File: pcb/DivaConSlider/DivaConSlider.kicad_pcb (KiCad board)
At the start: 2 copper layers, 548 x 97 mm, 225 parts, among them J1 HS96L03W2C03, J2 B8B-PH-SM4-TB, U1 MPR121QR2, U2 MPR121QR2, U3 MPR121QR2, U4 MPR121QR2, U5 74AHCT1G14

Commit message: revision 1.1 pcb schematics and layout
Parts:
- R17: value 330R -> 470R
- U5: value 74AHCT1G14 -> 74HCT1G14
- moved R5 8.00 mm to (96.0, 139.8)
- moved TP10 5.70 mm to (84.0, 145.0)
- moved R6 4.00 mm to (94.0, 139.8)
- moved TP11 3.75 mm to (79.8, 140.5)
- moved C13 3.32 mm to (88.0, 139.8), turned to -90 degrees
- moved C6 2.94 mm to (84.0, 139.8), turned to -90 degrees
- moved TP12 2.47 mm to (87.2, 148.2)
- moved R7 2.00 mm to (90.0, 139.8)
- moved R8 2.00 mm to (92.0, 139.8)
- moved C12 1.98 mm to (86.5, 139.8), turned to -90 degrees
- moved C7 1.49 mm to (82.5, 139.8), turned to -90 degrees
- renumbered C78 to C14, C14 to C15, C15 to C16, C16 to C17, C17 to C18, C18 to C19, C19 to C20, C20 to C21, C21 to C22, C22 to C23, C23 to C24, C24 to C25, C25 to C26, C26 to C27, C27 to C28, C28 to C29, C29 to C30, C30 to C31, C31 to C32, C32 to C33, C33 to C34, C34 to C35, C35 to C36, C36 to C37, C37 to C38, C38 to C39, C39 to C40, C40 to C41, C41 to C42, C42 to C43, C43 to C44, C44 to C45, C45 to C46, C46 to C47, C47 to C48, C48 to C49, C49 to C50, C50 to C51, C51 to C52, C52 to C53, C53 to C54, C54 to C55, C55 to C56, C56 to C57, C57 to C58, C58 to C59, C59 to C60, C60 to C61, C61 to C62, C62 to C63, C63 to C64, C64 to C65, C65 to C66, C66 to C67, C67 to C68, C68 to C69, C69 to C70, C70 to C71, C71 to C72, C72 to C73, C73 to C74, C74 to C75, C75 to C76, C76 to C77, C77 to C78, R2 to R1, R1 to R2, TP14 to TP1, TP1 to TP10, TP8 to TP11, TP9 to TP12, TP11 to TP13, TP5 to TP2, TP2 to TP3, TP3 to TP4, TP4 to TP5, TP7 to TP6, TP12 to TP7, TP6 to TP8, TP13 to TP9
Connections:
- J2 pad 1: GND -> Net-(J2-Pin_1)
- J2 pad 5: Net-(J2-Pin_5) -> +3V3
- J2 pad 6: /LED_DATA -> GND
- J2 pad 7: +3V3 -> +5V
- J2 pad 8: +5V -> /LED_DATA
- R5 pad 1: Net-(J2-Pin_5) -> Net-(J2-Pin_1)
- R5 pad 2: /I2C_SCL -> /DISPLAY_I2C_SCL
- R6 pad 1: Net-(J2-Pin_4) -> Net-(J2-Pin_2)
- R6 pad 2: /I2C_SDA -> /DISPLAY_I2C_SDA
- R7 pad 2: /DISPLAY_I2C_SDA -> /I2C_SCL
- R8 pad 1: Net-(J2-Pin_2) -> Net-(J2-Pin_4)
- R8 pad 2: /DISPLAY_I2C_SCL -> /I2C_SDA
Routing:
- net +5V: track 955.6 -> 977.3 mm
- net Net-(J2-Pin_5): track 6.50 -> 0.00 mm
- net Net-(J2-Pin_1): track 0.00 -> 6.50 mm
- net /LED_DATA: track 17.3 -> 12.6 mm, vias 2 -> 0
- net GND: track 828.8 -> 824.6 mm, vias 1320 -> 1439
- net /I2C_SCL: track 457.7 -> 460.0 mm
- net Net-(D1-DIN): track 57.9 -> 59.9 mm
- net /I2C_SDA: track 456.1 -> 457.8 mm
- net /DISPLAY_I2C_SDA: track 90.7 -> 89.7 mm
- net Net-(J2-Pin_4): track 6.50 -> 7.33 mm, vias 0 -> 2
- net Net-(J2-Pin_3): track 6.50 -> 7.33 mm

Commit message: Update PCBs to purchased revision
Main edit is using a ULN2003 NPN transistor array over discrete MOSFETs.
This was chosen because there was limited board space to put in
pull-down resistors on the board and it was complicating the single
layer routing. The PCB had to be expanded to 70x75mm anyways to
accommodate the SOIC ic anyways.

The schematics of the IO board were also updated to use net labels over
direct wiring. Due to the JST connectors and the Pi Pico schematic
symbol being mirrored, it was getting too difficult to have an
understandable schematic.

Minor edit was changing LED_DATA to nLED_DATA to signify that it is
an active low signal.
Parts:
- added R17: 10k, Resistor_SMD:R_0603_1608Metric, B.Cu at (74.8, 136.8)
- added SYM1: Logo_Open_Hardware_Small, Symbol:OSHW-Logo_5.7x6mm_SilkScreen, F.Cu at (394.0, 132.0)
- added SYM2: Leek, CustomLogos:Leek-Logo_6.3mm_Silkscreen, F.Cu at (388.0, 131.0)
- added TP14: TestPoint, TestPoint:TestPoint_Pad_D1.5mm, B.Cu at (155.8, 134.4)
- C12, C6: footprint Capacitor_SMD:C_0603_1608Metric -> Capacitor_SMD:C_0805_2012Metric
- H37, H38, H39, H40, H41, H42, H43, H44, H45: value Spacer_M3 -> Standoff_M3
- J2: value B8B-PH-SM4-TB -> B8B-PH-SM4-TBT
- U5: value 74HCT1G14 -> 74HCT1G14GV,125
- moved C7 1.00 mm to (81.5, 139.8)
- moved C12 0.53 mm to (86.0, 139.9)
- moved C6 0.53 mm to (83.5, 139.9)
- moved TP10 0.50 mm to (83.5, 145.0)
- moved TP11 0.25 mm to (79.5, 140.5)
- turned R10 to 45 degrees
- turned R11 to 45 degrees
- turned R9 to 45 degrees
- renumbered R17 to R18, R18 to R19, TP4 to TP2, TP5 to TP3, TP2 to TP4, TP3 to TP5
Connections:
- net /LED_DATA renamed /nLED_DATA
- H41 pad 1: (no net) -> unconnected-(H41-Pad1)
- H42 pad 1: (no net) -> unconnected-(H42-Pad1)
- H43 pad 1: (no net) -> unconnected-(H43-Pad1)
- H44 pad 1: (no net) -> unconnected-(H44-Pad1)
- H45 pad 1: (no net) -> unconnected-(H45-Pad1)
- R10 pad 1: Net-(U2-~{IRQ}) -> +3V3
- R10 pad 2: +3V3 -> Net-(U2-~{IRQ})
- R11 pad 1: Net-(U3-~{IRQ}) -> +3V3
- R11 pad 2: +3V3 -> Net-(U3-~{IRQ})
- R9 pad 1: Net-(U1-~{IRQ}) -> +3V3
- R9 pad 2: +3V3 -> Net-(U1-~{IRQ})
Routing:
- net +5V: track 977.3 -> 983.4 mm
- net GND: track 824.6 -> 829.4 mm, vias 1439 -> 1441
- net /nLED_DATA: track 12.6 -> 16.2 mm
- net +3V3: track 542.6 -> 544.7 mm
- net /I2C_SCL: track 460.0 -> 461.6 mm
- net /I2C_SDA: track 457.8 -> 459.2 mm
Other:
- board text added: "${TITLE} Rev. ${REVISION} ${ISSUE_DATE} ${COMPANY}"
- board text added: "DISPLAY SCL"
- board text added: "DISPLAY SDA"
- board text added: "LED DATA"
- board text added: "SLIDER SCL"
- board text added: "SLIDER SDA"
- board text added: "nDATA"
- board text removed: "${TITLE} Rev. ${REVISION} ${COMPANY} ${ISSUE_DATE}"

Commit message: Fix slider led_data silkscreen
Didn't indicate active low on the connector, had just "DATA" for the
test point, and had a redundant old silk screen label from a removed
test point location
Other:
- board text added: "LED_DATA"
- board text added: "nLED DATA"
- board text removed: "DATA"
- board text removed: "LED DATA"
- board text removed: "nDATA"
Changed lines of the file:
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@@
 	(title_block
 		(title "DivaCon Gold Slider")
-		(date "2025-11-14")
-		(rev "1.1")
+		(date "2025-11-21")
+		(rev "1.2")
 		(company "Alexander Knapik")
 	)
@@
 		)
 	)
-	(gr_text "LED DATA"
+	(gr_text "nLED DATA"
 		(at 82 127.75 270)
 		(layer "F.SilkS")
@@
 		)
 	)
-	(gr_text "DATA"
-		(at 28.25 163.75 0)
-		(layer "B.SilkS")
-		(effects
-			(font
-				(size 1.5 1.5)
-				(thickness 0.3)
-				(bold yes)
-			)
-			(justify mirror)
-		)
-	)
 	(gr_text "I2C: 0x5D"
 		(at 503 158.83 0)
@@
 		)
 	)
-	(gr_text "nDATA"
-		(at 71.736 148 90)
+	(gr_text "LED_DATA"
+		(at 71.736 150 90)
 		(layer "B.SilkS")
 		(effects

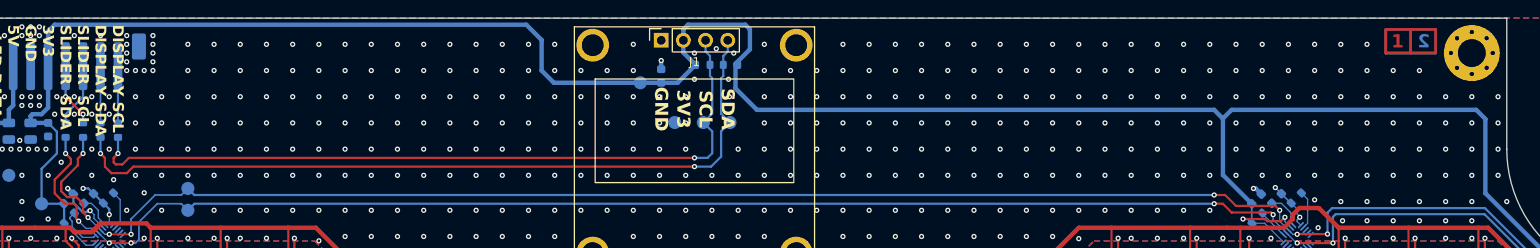
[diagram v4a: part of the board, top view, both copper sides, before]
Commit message: Generate slider PCB 3d model
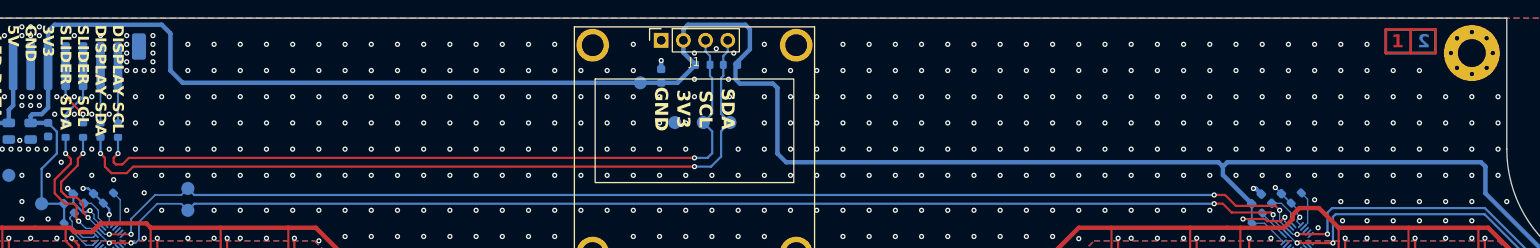
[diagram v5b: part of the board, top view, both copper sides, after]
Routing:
- net +3V3: track 544.7 -> 539.8 mm
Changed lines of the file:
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@@
 	)
 	(via
-		(at 161 136)
+		(at 162 136)
 		(size 0.6)
 		(drill 0.3)
@@
 	)
 	(segment
+		(start 103.4 134.4)
+		(end 102 133)
+		(width 0.508)
+		(layer "B.Cu")
+		(net 2)
+	)
+	(segment
+		(start 88.745 127.755)
+		(end 88 128.5)
+		(width 0.508)
+		(layer "B.Cu")
+		(net 2)
+	)
+	(segment
+		(start 222 143.5)
+		(end 172.5 143.5)
+		(width 0.508)
+		(layer "B.Cu")
+		(net 2)
+	)
+	(segment
 		(start 229.453204 152.665425)
 		(end 227.271142 150.483363)
@@
 	)
 	(segment
-		(start 166.698 132.222)
-		(end 168.35 130.57)
-		(width 0.508)
-		(layer "B.Cu")
-		(net 2)
-	)
-	(segment
-		(start 166.698 135.048)
-		(end 169.15 137.5)
-		(width 0.508)
-		(layer "B.Cu")
-		(net 2)
-	)
-	(segment
 		(start 89 139.995)
 		(end 89 142.5)
@@
 	)
 	(segment
-		(start 169.15 137.5)
-		(end 221.5 137.5)
+		(start 88 128.5)
+		(end 88 132.5)
 		(width 0.508)
 		(layer "B.Cu")
@@
 	)
 	(segment
-		(start 145.9 134.4)
-		(end 144.5 133)
+		(start 252.05 143.5)
+		(end 252.55 144)
 		(width 0.508)
 		(layer "B.Cu")
@@
 	)
 	(segment
+		(start 171 134.5)
+		(end 167.198 134.5)
+		(width 0.508)
+		(layer "B.Cu")
+		(net 2)
+	)
+	(segment
 		(start 498.856021 151.50611)
 		(end 497.833274 150.483363)
@@
 	)
 	(segment
-		(start 252.55 138.55)
-		(end 251.5 137.5)
+		(start 158.19 134.4)
+		(end 103.4 134.4)
 		(width 0.508)
 		(layer "B.Cu")
@@
 	)
 	(segment
-		(start 88.745 127.755)
-		(end 88 128.5)
+		(start 171.5 135)
+		(end 171 134.5)
 		(width 0.508)
 		(layer "B.Cu")
@@
 	)
 	(segment
-		(start 144.5 133)
-		(end 144.5 129.5)
+		(start 168.35 128.284)
+		(end 167.821 127.755)
 		(width 0.508)
 		(layer "B.Cu")
@@
 	)
 	(segment
+		(start 168.35 130.57)
+		(end 168.35 128.284)
+		(width 0.508)
+		(layer "B.Cu")
+		(net 2)
+	)
+	(segment
 		(start 361.8 144.2)
 		(end 361.8 148.25)
@@
 	)
 	(segment
-		(start 160.076 134.4)
-		(end 162.128 132.348)
+		(start 223 143.5)
+		(end 252.05 143.5)
 		(width 0.508)
 		(layer "B.Cu")
@@
 	)
 	(segment
-		(start 166.698 132.348)
-		(end 166.698 135.048)
+		(start 172.5 143.5)
+		(end 171.5 142.5)
 		(width 0.508)
 		(layer "B.Cu")
@@
 	)
 	(segment
-		(start 222.5 138.5)
+		(start 160.076 134.4)
+		(end 162.128 132.348)
+		(width 0.508)
+		(layer "B.Cu")
+		(net 2)
+	)
+	(segment
+		(start 222.5 144)
 		(end 222.5 144.95)
 		(width 0.508)
@@
 	)
 	(segment
+		(start 222.5 144)
+		(end 222 143.5)
+		(width 0.508)
+		(layer "B.Cu")
+		(net 2)
+	)
+	(segment
 		(start 495.549822 148.25)
 		(end 494.649911 147.350089)
@@
 	)
 	(segment
+		(start 167.198 134.5)
+		(end 166.698 134)
+		(width 0.508)
+		(layer "B.Cu")
+		(net 2)
+	)
+	(segment
 		(start 227.271142 150.483363)
 		(end 225.766637 150.483363)
@@
 	)
 	(segment
-		(start 88 128.5)
-		(end 88 132.5)
+		(start 160.73 128.284)
+		(end 160.73 129.54)
+		(width 0.508)
+		(layer "B.Cu")
+		(net 2)
+	)
+	(segment
+		(start 171.5 142.5)
+		(end 171.5 135)
 		(width 0.508)
 		(layer "B.Cu")
@@
 	)
 	(segment
+		(start 161.259 127.755)
+		(end 160.73 128.284)
+		(width 0.508)
+		(layer "B.Cu")
+		(net 2)
+	)
+	(segment
 		(start 88 132.5)
 		(end 88 137.25)
@@
 	)
 	(segment
-		(start 144.5 129.5)
-		(end 142.755 127.755)
-		(width 0.508)
-		(layer "B.Cu")
-		(net 2)
-	)
-	(segment
 		(start 499 145.950308)
 		(end 497.8 147.150308)
@@
 	)
 	(segment
-		(start 251.5 137.5)
-		(end 223.5 137.5)
-		(width 0.508)
-		(layer "B.Cu")
-		(net 2)
-	)
-	(segment
-		(start 221.5 137.5)
-		(end 222.5 138.5)
+		(start 167.821 127.755)
+		(end 161.259 127.755)
 		(width 0.508)
 		(layer "B.Cu")
@@
 	)
 	(segment
-		(start 223.5 137.5)
-		(end 222.5 138.5)
-		(width 0.508)
-		(layer "B.Cu")
-		(net 2)
-	)
-	(segment
 		(start 87.25 148.25)
 		(end 89.8 148.25)
@@
 	)
 	(segment
-		(start 167.821 127.755)
-		(end 168.35 128.284)
-		(width 0.508)
-		(layer "B.Cu")
-		(net 2)
-	)
-	(segment
 		(start 336.5 156)
 		(end 335.5 156)
@@
 	)
 	(segment
-		(start 142.755 127.755)
+		(start 101 127.755)
 		(end 88.745 127.755)
 		(width 0.508)
@@
 	)
 	(segment
-		(start 161.259 127.755)
-		(end 167.821 127.755)
+		(start 166.698 134)
+		(end 166.698 132.222)
 		(width 0.508)
 		(layer "B.Cu")
@@
 	)
 	(segment
+		(start 102 128.755)
+		(end 101 127.755)
+		(width 0.508)
+		(layer "B.Cu")
+		(net 2)
+	)
+	(segment
 		(start 359.25 146.25)
 		(end 346.25 146.25)
@@
 	)
 	(segment
-		(start 166.698 132.348)
-		(end 166.698 132.222)
+		(start 252.55 147.05)
+		(end 252.55 144)
 		(width 0.508)
 		(layer "B.Cu")
@@
 	)
 	(segment
+		(start 102 133)
+		(end 102 128.755)
+		(width 0.508)
+		(layer "B.Cu")
+		(net 2)
+	)
+	(segment
 		(start 225.2984 150)
 		(end 225.781763 150.483363)
@@
 	)
 	(segment
-		(start 158.19 134.4)
-		(end 145.9 134.4)
-		(width 0.508)
-		(layer "B.Cu")
-		(net 2)
-	)
-	(segment
 		(start 332.45 159.8)
 		(end 264.8 159.8)
@@
 	)
 	(segment
-		(start 160.73 128.284)
-		(end 161.259 127.755)
-		(width 0.508)
-		(layer "B.Cu")
-		(net 2)
-	)
-	(segment
 		(start 364.3 140.5)
 		(end 363.4 141.4)
@@
 	)
 	(segment
-		(start 252.55 147.05)
-		(end 252.55 138.55)
-		(width 0.508)
-		(layer "B.Cu")
-		(net 2)
-	)
-	(segment
-		(start 160.73 129.54)
-		(end 160.73 128.284)
+		(start 222.5 144)
+		(end 223 143.5)
 		(width 0.508)
 		(layer "B.Cu")
@@
 	)
 	(segment
-		(start 222.5 144.95)
-		(end 225.8 148.25)
+		(start 166.698 132.222)
+		(end 168.35 130.57)
 		(width 0.508)
 		(layer "B.Cu")
@@
 	)
 	(segment
-		(start 168.35 128.284)
-		(end 168.35 130.57)
+		(start 222.5 144.95)
+		(end 225.8 148.25)
 		(width 0.508)
 		(layer "B.Cu")
